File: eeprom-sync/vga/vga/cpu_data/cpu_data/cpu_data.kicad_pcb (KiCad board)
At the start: 2 copper layers, 81.3 x 43.2 mm, 33 parts, among them J1 Conn_02x06_Odd_Even, J10 Conn_01x03_Female, J11 Conn_01x02_Female, J12 Conn_02x05_Odd_Even, J2 Conn_01x02_Female, J3 Conn_01x04_Female, J4 Conn_01x15_Female, J5 Conn_01x15_Female, J6 Conn_02x08_Odd_Even, J7 Conn_01x02_Female, J8 Conn_01x02_Female, J9 Conn_01x08_Female, Q1 Q_PMOS_GSD, U1 GAL22V10, U2 74HC14, U3 74LS02, U4 IDT7205L12JG, U5 74LS573

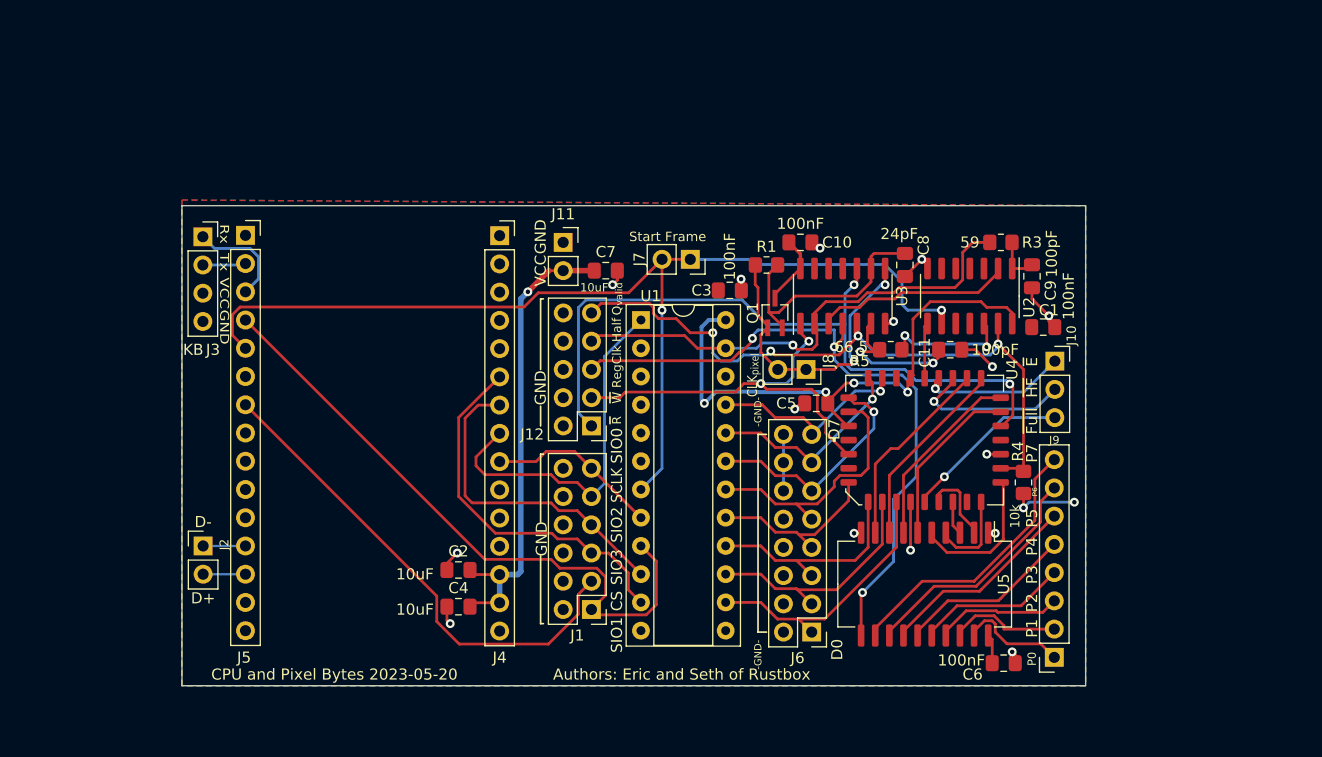
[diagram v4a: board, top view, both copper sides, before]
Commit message: adding the socket  footprint
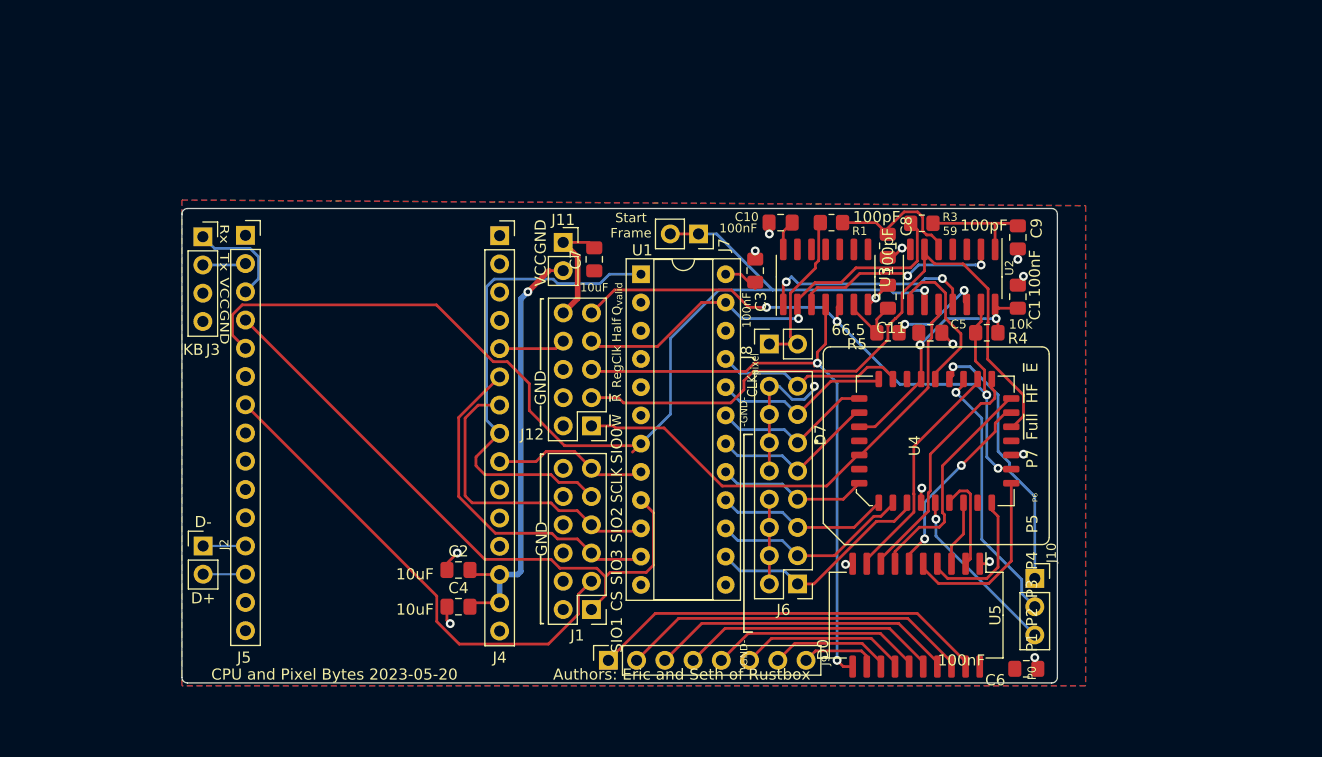
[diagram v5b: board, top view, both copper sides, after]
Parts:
- removed Q1: Q_PMOS_GSD, Package_TO_SOT_SMD:SOT-323_SC-70_Handsoldering
- C8: value 24pF -> 100pF
- U4: footprint Package_LCC:PLCC-32_11.4x14.0mm_P1.27mm -> plcc32:plcc32-socket
- moved J9 40.1 mm to (114.6, 101.3), turned to 90 degrees
- moved J10 19.6 mm to (152.9, 94.0)
- moved R4 13.9 mm to (148.6, 71.9), turned to 0 degrees
- moved C5 12.1 mm to (143.5, 71.9), turned to 180 degrees
- moved C11 7.36 mm to (139.7, 68.6), turned to 90 degrees
- moved R3 7.32 mm to (142.7, 62.0)
- moved R1 6.97 mm to (134.6, 62.0)
- moved J6 4.52 mm to (131.6, 94.5)
- moved U1 4.12 mm to (117.5, 66.6)
- moved J8 4.02 mm to (129.0, 72.9), turned to 90 degrees
- moved C9 3.72 mm to (151.4, 63.3)
- moved C1 3.57 mm to (151.4, 68.6), turned to -90 degrees
- moved C3 2.90 mm to (127.8, 66.3), turned to -90 degrees
- moved U5 2.90 mm to (142.2, 97.3)
- moved C10 2.51 mm to (130.0, 62.0), turned to 0 degrees
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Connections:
- C8 pad 1: Net-(C8-Pad1) -> Net-(R1-Pad2)
- J12 pad 1: /~{R} -> /~{W}
- J12 pad 3: /~{W} -> /~{R}
- R1 pad 2: Net-(C8-Pad1) -> Net-(R1-Pad2)
- U2 pad 10: (no net) -> /~{W}
- U2 pad 11: (no net) -> Net-(U3-Pad1)
- U2 pad 5: (no net) -> Net-(R1-Pad2)
- U2 pad 6: (no net) -> /~{R}
- U3 pad 1: /~{W} -> Net-(U3-Pad1)
- U3 pad 10: /~{R} -> (no net)
- U3 pad 8: /CLK_{pixel} -> (no net)
- U3 pad 9: Net-(C8-Pad1) -> (no net)
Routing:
- net VCC: track 108.6 -> 70.0 mm, vias 7 -> 3
- net /P0: track 9.79 -> 36.1 mm
- net Net-(C8-Pad1): track 22.2 -> 0.00 mm
- net /P1: track 10.1 -> 31.9 mm
- net GND: track 34.5 -> 55.0 mm
- net Net-(U3-Pad1): track 0.00 -> 19.8 mm, vias 0 -> 2
- net /P7: track 25.2 -> 6.95 mm
- net /P2: track 11.4 -> 27.7 mm
- net /CLK_{pixel}: track 27.9 -> 14.8 mm, vias 2 -> 0
- net Net-(R1-Pad2): track 0.00 -> 12.7 mm
- net /Empty: track 13.1 -> 24.2 mm
- net /SCLK: track 33.1 -> 44.1 mm
- net /P6: track 21.6 -> 11.0 mm
- net /P3: track 13.6 -> 23.5 mm
- net /Reset: track 5.02 -> 14.2 mm
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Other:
- board size 81.3 x 43.2 mm -> 78.7 x 42.7 mm
- board text removed: "."

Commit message: routing completed
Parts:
- moved J2 56.5 mm to (134.6, 91.4)
- moved J3 45.8 mm to (106.7, 99.1), turned to 90 degrees
- moved J10 33.9 mm to (119.4, 99.1), turned to 90 degrees
- moved J9 32.8 mm to (147.3, 101.6), turned to -90 degrees
- moved J4 26.0 mm to (78.8, 63.5)
- moved C9 21.3 mm to (131.3, 70.4), turned to 90 degrees
- moved J5 19.7 mm to (101.6, 63.5)
- moved C2 18.5 mm to (82.5, 93.7), turned to 180 degrees
- moved C4 18.5 mm to (82.5, 97.0), turned to 180 degrees
- moved J1 17.0 mm to (106.7, 81.0), turned to 0 degrees
- moved R3 15.8 mm to (129.3, 70.3), turned to -90 degrees
- moved R5 15.0 mm to (124.7, 71.6), turned to -90 degrees
- moved C5 14.3 mm to (129.3, 73.4), turned to 0 degrees
- moved J8 13.9 mm to (121.9, 61.0)
- moved C11 12.8 mm to (127.0, 70.3)
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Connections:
- J1 pad 1: /SIO1 -> GND
- J1 pad 10: GND -> /SCLK
- J1 pad 11: /SIO0 -> GND
- J1 pad 12: GND -> /SIO0
- J1 pad 2: GND -> /SIO1
- J1 pad 3: /CS -> GND
- J1 pad 4: GND -> /CS
- J1 pad 5: /SIO3 -> GND
- J1 pad 6: GND -> /SIO3
- J1 pad 7: /SIO2 -> GND
- J1 pad 8: GND -> /SIO2
- J1 pad 9: /SCLK -> GND
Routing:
- net /SIO0: track 13.8 -> 57.8 mm
- net /D-: track 3.81 -> 38.2 mm
- net /D+: track 3.81 -> 37.8 mm
- net /CS: track 44.8 -> 11.4 mm
- net /KB_{Tx}: track 3.89 -> 36.1 mm
- net /SIO1: track 56.5 -> 24.6 mm
- net /SCLK: track 44.1 -> 74.8 mm
- net /P0: track 36.1 -> 5.96 mm
- net /Empty: track 24.2 -> 51.8 mm
- net /KB_{Rx}: track 9.39 -> 35.9 mm
- net /P1: track 31.9 -> 6.49 mm
- net Net-(R5-Pad2): track 8.94 -> 30.1 mm
- net /P2: track 27.7 -> 8.06 mm
- net Net-(C9-Pad1): track 10.1 -> 29.7 mm, vias 0 -> 2
- net /SIO2: track 27.6 -> 47.2 mm
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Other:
- board size 78.7 x 42.7 mm -> 78.7 x 44.7 mm

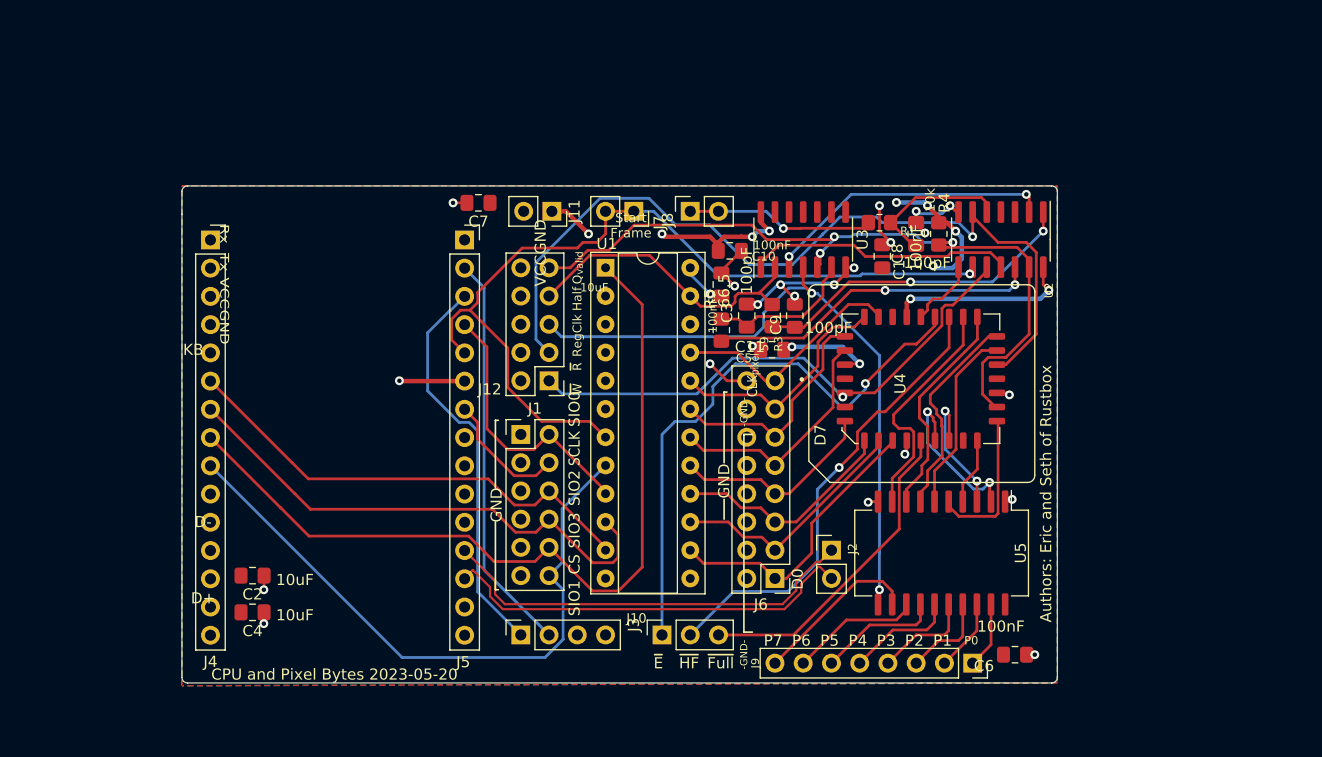
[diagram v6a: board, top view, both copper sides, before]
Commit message: labels on the back of the board, layout and retraced, labels on front of board
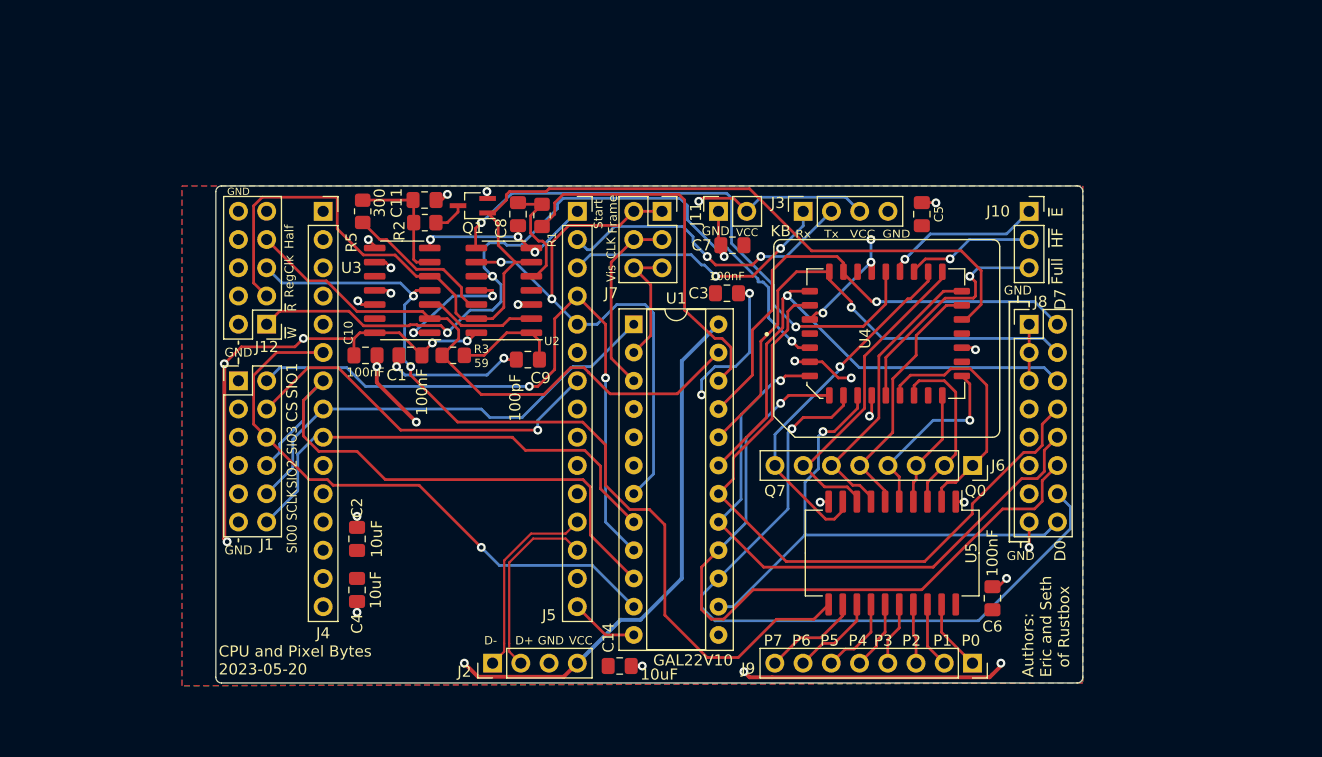
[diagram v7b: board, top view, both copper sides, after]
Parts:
- removed R4: 10k, Resistor_SMD:R_0805_2012Metric_Pad1.20x1.40mm_HandSolder
- added C14: 10uF, Capacitor_SMD:C_0805_2012Metric_Pad1.18x1.45mm_HandSolder, F.Cu at (115.6, 101.9)
- added Q1: Q_NMOS_GSD, Package_TO_SOT_SMD:SOT-323_SC-70_Handsoldering, F.Cu at (102.4, 60.5)
- added R2: 50, Resistor_SMD:R_0805_2012Metric_Pad1.20x1.40mm_HandSolder, F.Cu at (98.0, 62.0)
- J2: value Conn_01x02_Female -> Conn_01x04_Male; footprint Connector_PinHeader_2.54mm:PinHeader_1x02_P2.54mm_Vertical -> Connector_PinHeader_2.54mm:PinHeader_1x04_P2.54mm_Vertical
- J6: value Conn_02x08_Odd_Even -> Conn_01x08_Female; footprint Connector_PinHeader_2.54mm:PinHeader_2x08_P2.54mm_Vertical -> Connector_PinSocket_2.54mm:PinSocket_1x08_P2.54mm_Vertical
- J7: value Conn_01x02_Female -> Conn_02x03_Odd_Even; footprint Connector_PinSocket_2.54mm:PinSocket_1x02_P2.54mm_Vertical -> Connector_PinSocket_2.54mm:PinSocket_2x03_P2.54mm_Vertical
- J8: value Conn_01x02_Female -> Conn_02x08_Odd_Even; footprint Connector_PinSocket_2.54mm:PinSocket_1x02_P2.54mm_Vertical -> Connector_PinHeader_2.54mm:PinHeader_2x08_P2.54mm_Vertical
- R5: value 66.5 -> 300
- moved J10 50.4 mm to (152.4, 61.0), turned to 0 degrees
- moved J3 45.8 mm to (132.1, 61.0)
- moved U2 44.9 mm to (105.2, 68.1), turned to 180 degrees
- moved C1 43.4 mm to (96.8, 73.9), turned to 0 degrees
- moved U3 36.4 mm to (96.0, 68.1), turned to 180 degrees
- moved C8 35.9 mm to (106.4, 61.2), turned to -90 degrees
- moved C10 34.1 mm to (92.7, 73.9)
- moved R5 34.0 mm to (92.5, 61.0)
- moved J8 32.1 mm to (152.4, 71.1), turned to 0 degrees
- moved J2 32.1 mm to (104.1, 101.6), turned to 90 degrees
- moved C11 30.8 mm to (98.0, 59.9), turned to 0 degrees
- moved R1 30.4 mm to (108.6, 61.3), turned to 90 degrees
- moved R3 28.9 mm to (100.6, 73.9), turned to 0 degrees
- moved J12 25.9 mm to (83.8, 71.1)
- moved J1 25.9 mm to (81.3, 76.2)
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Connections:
- J12 pad 9: /Q_{valid} -> unconnected-(J12-Pad9)
- J6 pad 1: /D0 -> /Q0
- J6 pad 2: GND -> /Q1
- J6 pad 3: /D1 -> /Q2
- J6 pad 4: GND -> /Q3
- J6 pad 5: /D2 -> /Q4
- J6 pad 6: GND -> /Q5
- J6 pad 7: /D3 -> /Q6
- J6 pad 8: GND -> /Q7
- J8 pad 1: /CLK_{pixel} -> GND
- J8 pad 2: /CLK_{pixel} -> /D7
- U1 pad 2: unconnected-(U1-Pad2) -> /Vis
- U1 pad 22: unconnected-(U1-Pad22) -> /CLK_{pixel}
- U1 pad 3: unconnected-(U1-Pad3) -> /CLK
- U2 pad 13: /Q_{valid} -> /~{R}
- U2 pad 3: (no net) -> GND
- U2 pad 4: (no net) -> unconnected-(U2-Pad4)
- U3 pad 10: (no net) -> unconnected-(U3-Pad10)
- U3 pad 11: (no net) -> GND
- U3 pad 12: (no net) -> GND
- U3 pad 13: (no net) -> unconnected-(U3-Pad13)
- U3 pad 5: /Q_{valid} -> /~{R}
- U3 pad 8: (no net) -> GND
- U3 pad 9: (no net) -> GND
- U4 pad 15: /Q_{valid} -> unconnected-(U4-Pad15)
- U4 pad 3: unconnected-(U4-Pad3) -> GND
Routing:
- net VCC: track 56.2 -> 142.1 mm
- net /Q_{valid}: track 68.9 -> 0.00 mm, vias 3 -> 0
- net /Reset: track 6.33 -> 52.1 mm, vias 0 -> 2
- net /D2: track 20.4 -> 65.3 mm, vias 0 -> 1
- net /D1: track 22.4 -> 66.6 mm, vias 0 -> 1
- net GND: track 52.9 -> 93.8 mm, vias 23 -> 29
- net /D4: track 21.7 -> 61.5 mm
- net /D3: track 18.6 -> 56.2 mm, vias 0 -> 1
- net /Empty: track 51.8 -> 14.3 mm
- net /SIO1: track 24.6 -> 60.1 mm, vias 0 -> 2
- net /SCLK: track 74.8 -> 41.5 mm
- net /HalfFull: track 41.5 -> 11.6 mm
- net /~{R}: track 76.6 -> 104.3 mm, vias 1 -> 0
- net /D5: track 21.1 -> 47.6 mm, vias 0 -> 1
- net /Half: track 27.6 -> 53.4 mm
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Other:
- board size 78.7 x 44.7 mm -> 78 x 44.7 mm
- board text added: "CLK"
- board text added: "GAL22V10"
- board text added: "J1"
- board text added: "J10"
- board text added: "J11"
- board text added: "J12"
- board text added: "J2"
- board text added: "J3"
- board text added: "J4"
- board text added: "J5"
- board text added: "J6"
- board text added: "J8"
- board text added: "J9"
- board text added: "Q0"
- board text added: "Q7"
- board text added: "U1"
- board text added: "Vis"
- board text removed: "-GND-"
- board text removed: "100nF"
- board text removed: "10uF"
- board text removed: "CLK_{pixel}"
- board text removed: "Q_{valid}"

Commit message: updating gal to include the pixel clk output as expressed in the scchematic
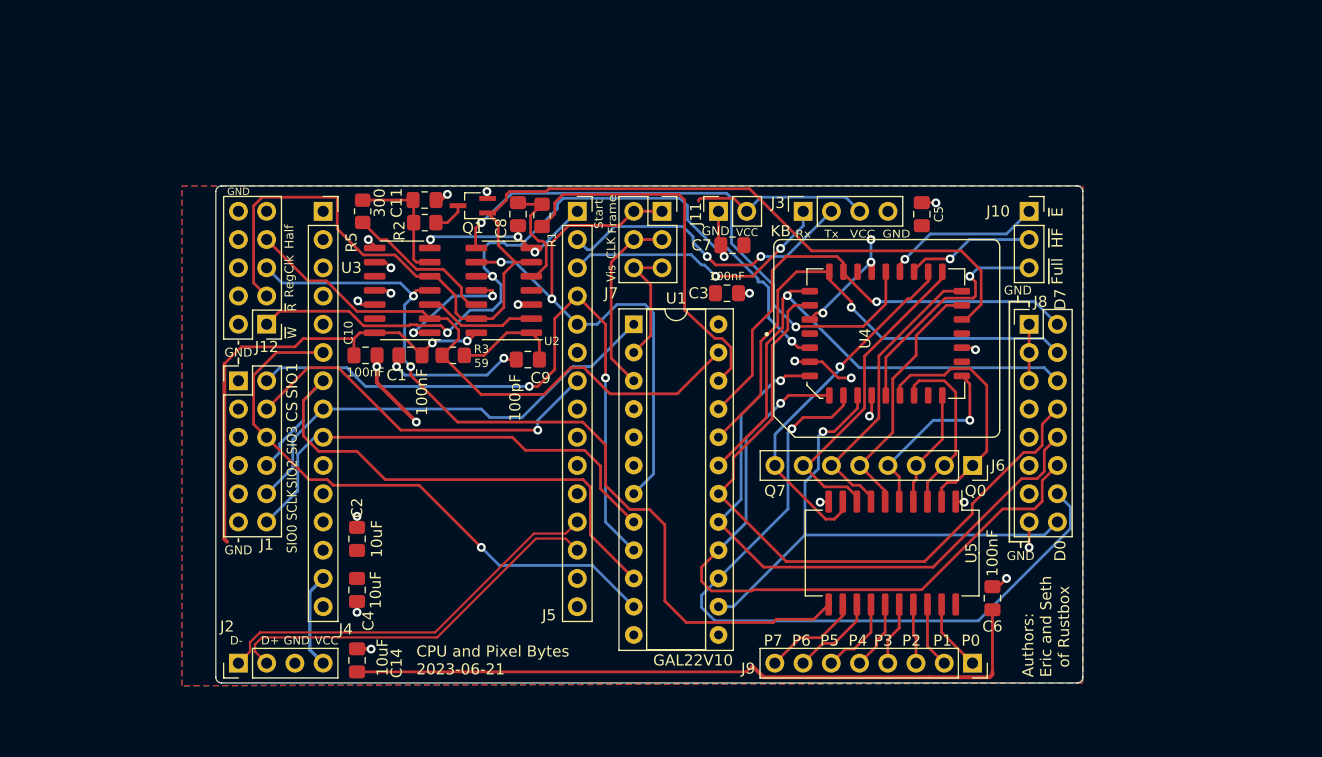
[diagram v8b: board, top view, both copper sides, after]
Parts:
- moved C14 23.6 mm to (91.9, 101.3), turned to -90 degrees
- moved J2 22.9 mm to (81.3, 101.6)
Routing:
- net /D-: track 17.7 -> 36.2 mm
- net /D+: track 16.9 -> 35.5 mm
- net GND: track 93.8 -> 75.8 mm, vias 29 -> 28
- net /D2: track 65.3 -> 61.7 mm
- net /RegClk: track 80.7 -> 77.4 mm
- net VCC: track 142.1 -> 142.5 mm, vias 12 -> 5
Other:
- board text added: "CPU and Pixel Bytes 2023-06-21"
- board text removed: "CPU and Pixel Bytes 2023-05-20"
